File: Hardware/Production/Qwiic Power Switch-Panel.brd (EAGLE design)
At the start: 149.1 x 149.1 mm, 1505 parts, among them J1 Qwiic Right Angle, J10 PTH, J100 PTH, J103 Qwiic Right Angle, J104 PTH, J105 Qwiic Right Angle, J106 PTH, J109 Qwiic Right Angle, J110 PTH, J111 Qwiic Right Angle, J112 PTH, J115 Qwiic Right Angle, J116 PTH, J117 Qwiic Right Angle, J118 PTH, J121 Qwiic Right Angle, J122 PTH, J123 Qwiic Right Angle, J124 PTH, J127 Qwiic Right Angle, J128 PTH, J129 Qwiic Right Angle, J13 Qwiic Right Angle, J130 PTH, J133 Qwiic Right Angle, J134 PTH, J135 Qwiic Right Angle, J136 PTH, J139 Qwiic Right Angle, J14 PTH, J140 PTH, J141 Qwiic Right Angle, J142 PTH, J145 Qwiic Right Angle, J146 PTH, J147 Qwiic Right Angle, J148 PTH, J15 Qwiic Right Angle, J16 PTH, J19 Qwiic Right Angle, J2 PTH, J20 PTH, J21 Qwiic Right Angle, J22 PTH, J25 Qwiic Right Angle, J26 PTH, J27 Qwiic Right Angle, J28 PTH, J3 Qwiic Right Angle, J31 Qwiic Right Angle, J32 PTH, J33 Qwiic Right Angle, J34 PTH, J37 Qwiic Right Angle, J38 PTH, J39 Qwiic Right Angle, J4 PTH, J40 PTH, J43 Qwiic Right Angle, J44 PTH, J45 Qwiic Right Angle, J46 PTH, J49 Qwiic Right Angle, J50 PTH, J51 Qwiic Right Angle, J52 PTH, J55 Qwiic Right Angle, J56 PTH, J57 Qwiic Right Angle, J58 PTH, J61 Qwiic Right Angle, J62 PTH, J63 Qwiic Right Angle, J64 PTH, J67 Qwiic Right Angle, J68 PTH, J69 Qwiic Right Angle, J7 Qwiic Right Angle, J70 PTH, J73 Qwiic Right Angle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

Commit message: Add x02 production files
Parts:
- added I2C_OUT, I2C_OUT1, I2C_OUT10, I2C_OUT11, I2C_OUT12, I2C_OUT13, I2C_OUT14, I2C_OUT15, I2C_OUT16, I2C_OUT17, I2C_OUT18, I2C_OUT19, I2C_OUT2, I2C_OUT20, I2C_OUT21, I2C_OUT22, I2C_OUT23, I2C_OUT24, I2C_OUT3, I2C_OUT4, I2C_OUT5, I2C_OUT6, I2C_OUT7, I2C_OUT8, I2C_OUT9: JUMPER-SMT_3_2-NC_TRACE_SILK, SparkFun-Jumpers:SMT-JUMPER_3_2-NC_TRACE_SILK
- added R126, R127, R129, R130, R134, R135, R137, R138, R142, R143, R145, R146, R150, R151, R153, R154, R158, R159, R161, R162, R166, R167, R169, R170, R174, R175, R177, R178, R182, R183, R185, R186, R190, R191, R193, R194, R198, R199: 2.2k, SparkFun-Resistors:0603
- added R128, R136, R144, R152, R160, R168, R176, R184, R192, R200: 200k, SparkFun-Resistors:0603
- added R131, R133, R139, R141, R147, R149, R155, R157, R163, R165, R171, R173, R179, R181, R187, R189, R195, R197: 1k, SparkFun-Resistors:0603
- added R132, R140, R148, R156, R164, R172, R180, R188, R196: 470, SparkFun-Resistors:0603
- added U$776, U$800: (no value), Labels:I_SUPER2_C-()-03
- added U$777, U$780: (no value), Labels-0_04:GND1
- added U$778, U$782: (no value), Labels-0_04:SCL9
- added U$779, U$781: (no value), Labels-0_04:SDA8
- added U$783: (no value), Qwiic:QWIIC0
- added U$784, U$797: (no value), 3.3V_Flagtail:3#3V0
- added U$785, U$796: (no value), 3.3V_Pointer:3#3V0
- added U$786, U$794: (no value), GPIO1:GPIO10
- added U$787, U$795: (no value), GPIO2:GPIO20
- added U$788: (no value), IN:IN0
- added U$789: (no value), LED_IN:LED_IN0
- added U$790: (no value), LED_OUT:LED_OUT0
- added U$791: (no value), OUT:OUT0
- added U$792: (no value), Power:POWER0
- added U$793: (no value), Switch:SWITCH0
- added U$798: (no value), IN__3:IN0
- added U$799: (no value), OUT__3:OUT0
- added U51, U54, U57, U60, U63, U66, U69, U72, U75: (no value), SparkFun-IC-Comms:VSSOP_8PIN
- added U52, U55, U58, U61, U64, U67, U70, U73: PCA9536, New_Parts:MSOP8
- added U53, U56, U59, U62, U65, U68, U71, U74: 74HC1G04, SparkFun-IC-Logic:SOT353
- R10, R103, R105, R110, R113, R114, R118, R119, R14, R15, R18, R23, R25, R30, R33, R34, R38, R39, R49, R50, R54, R55, R58, R63, R65, R70, R73, R74, R78, R79, R89, R9, R90, R94, R95, R98: value 1k -> 2.2k
- R100, R108, R124, R2, R20, R28, R44, R60, R68, R84: value 1k -> 470
- R101, R107, R11, R117, R21, R27, R37, R51, R61, R67, R77, R91: value 2.2k -> 1k
- R104, R120, R24, R40, R48, R64, R8, R80, R88: value 1k -> 200k
- R112, R16, R32, R56, R72, R96: value 2.2k -> 200k
- R116, R12, R36, R52, R76, R92: value 2.2k -> 470
- U$1, U$94: value SPARKX-LOGO4 -> (none); device SparkX:SPARKX-MEDIUM -> IN__3:IN0
- U$100, U$107, U$134, U$196, U$262, U$324, U$38, U$45, U$685, U$747: device Labels-0_04:SCL9 -> Labels-0_04:SDA8
- U$101, U$194: device Labels:I_SUPER2_C-()-03 -> Labels-0_04:GND1
- U$102, U$164, U$198, U$260, U$36, U$43, U$653, U$715, U$749: device Labels-0_04:GND1 -> Labels-0_04:SDA8
- U$104, U$128, U$168, U$192, U$352, U$416: device Labels-0_04:SDA8 -> Labels:I_SUPER2_C-()-03
- U$106, U$135, U$199, U$259, U$323, U$35, U$42, U$686, U$750, U$99: device Labels-0_04:SDA8 -> Labels-0_04:SCL9
- U$108, U$201, U$325, U$418: device Qwiic:QWIIC0 -> Labels-0_04:GND1
- U$109, U$171, U$326, U$388, U$525, U$587, U$742: device 3.3V_Flagtail:3#3V0 -> Labels-0_04:SDA8
- U$110, U$234, U$327, U$451, U$462, U$586, U$679: device 3.3V_Pointer:3#3V0 -> Labels-0_04:SCL9
- U$111, U$367: device GPIO1:GPIO10 -> Qwiic:QWIIC0
- U$112, U$368, U$701: device GPIO2:GPIO20 -> 3.3V_Flagtail:3#3V0
- U$113, U$433, U$764, U$92: device IN:IN0 -> 3.3V_Pointer:3#3V0
- U$114: device LED_IN:LED_IN0 -> GPIO1:GPIO10
- U$115: device LED_OUT:LED_OUT0 -> GPIO2:GPIO20
- U$116, U$372: device OUT:OUT0 -> IN:IN0
- U$117: device Power:POWER0 -> LED_IN:LED_IN0
- U$118: device Switch:SWITCH0 -> LED_OUT:LED_OUT0
- U$119: device GPIO1:GPIO10 -> OUT:OUT0
- U$120: device GPIO2:GPIO20 -> Power:POWER0
- U$121, U$761: device 3.3V_Pointer:3#3V0 -> Switch:SWITCH0
- U$122, U$370, U$698: device 3.3V_Flagtail:3#3V0 -> GPIO1:GPIO10
- U$123, U$371, U$51: device IN:IN0 -> GPIO2:GPIO20
- U$124, U$209, U$465: device OUT:OUT0 -> 3.3V_Pointer:3#3V0
- U$125, U$528: value SPARKX-LOGO4 -> (none); device SparkX:SPARKX-MEDIUM -> 3.3V_Flagtail:3#3V0
- U$126, U$222, U$350, U$446: device Labels-0_04:GND1 -> IN__3:IN0
- U$127, U$255, U$351, U$479: device Labels-0_04:SCL9 -> OUT__3:OUT0
- U$129, U$257, U$353: value (none) -> SPARKX-LOGO4; device Labels-0_04:GND1 -> SparkX:SPARKX-MEDIUM
- U$130, U$137, U$197, U$261, U$290, U$354, U$37, U$44, U$66, U$73, U$748: device Labels-0_04:SDA8 -> Labels-0_04:GND1
- U$132, U$70: device Labels:I_SUPER2_C-()-03 -> Labels-0_04:SDA8
- U$136, U$160, U$18, U$288, U$384, U$40, U$64: device Labels-0_04:GND1 -> Labels:I_SUPER2_C-()-03
- U$139, U$294, U$356, U$77: device Qwiic:QWIIC0 -> Labels-0_04:SDA8
- U$14, U$671: device IN:IN0 -> OUT__3:OUT0
- U$140, U$233, U$357, U$450, U$556, U$649, U$773: device 3.3V_Flagtail:3#3V0 -> Labels-0_04:GND1
- U$141, U$203, U$358, U$420, U$493, U$555, U$710, U$772: device 3.3V_Pointer:3#3V0 -> Labels-0_04:SDA8
- U$142, U$266, U$359, U$398, U$483, U$522, U$615, U$739: device GPIO1:GPIO10 -> Labels-0_04:SCL9
- U$143, U$399: device GPIO2:GPIO20 -> Qwiic:QWIIC0
- U$144, U$464, U$61, U$733: device IN:IN0 -> 3.3V_Flagtail:3#3V0
- U$145: device LED_IN:LED_IN0 -> 3.3V_Pointer:3#3V0
- U$146: device LED_OUT:LED_OUT0 -> GPIO1:GPIO10
- U$147, U$155, U$403: device OUT:OUT0 -> GPIO2:GPIO20
- U$148: device Power:POWER0 -> IN:IN0
- U$149: device Switch:SWITCH0 -> LED_IN:LED_IN0
- U$150: device GPIO1:GPIO10 -> LED_OUT:LED_OUT0
- U$151: device GPIO2:GPIO20 -> OUT:OUT0
- U$152: device 3.3V_Pointer:3#3V0 -> Power:POWER0
- U$153, U$729: device 3.3V_Flagtail:3#3V0 -> Switch:SWITCH0
- U$154, U$402, U$82: device IN:IN0 -> GPIO1:GPIO10
- U$156, U$497: value SPARKX-LOGO4 -> (none); device SparkX:SPARKX-MEDIUM -> 3.3V_Pointer:3#3V0
- U$157, U$253, U$381, U$477, U$560, U$656: device Labels-0_04:GND1 -> 3.3V_Flagtail:3#3V0
- U$158, U$286, U$382, U$510: device Labels-0_04:SCL9 -> IN__3:IN0
- U$159, U$223, U$383, U$447: device Labels-0_04:SDA8 -> OUT__3:OUT0
- U$161, U$321, U$385, U$97: value (none) -> SPARKX-LOGO4; device Labels-0_04:SDA8 -> SparkX:SPARKX-MEDIUM
- U$162, U$165, U$169, U$258, U$293, U$33, U$386, U$41, U$69, U$716, U$76: device Labels-0_04:SCL9 -> Labels-0_04:GND1
- U$163, U$39: device Labels:I_SUPER2_C-()-03 -> Labels-0_04:SCL9
- U$167, U$195, U$291, U$622, U$67, U$71, U$718, U$74, U$746: device Labels-0_04:GND1 -> Labels-0_04:SCL9
- U$170, U$263, U$387, U$46: device Qwiic:QWIIC0 -> Labels-0_04:SCL9
- U$172, U$265, U$389, U$482, U$524, U$617, U$741: device 3.3V_Pointer:3#3V0 -> Labels-0_04:GND1
- U$173, U$235, U$390, U$429, U$452, U$491, U$646, U$708: device GPIO1:GPIO10 -> Labels-0_04:SDA8
- U$174, U$298, U$391, U$430, U$515, U$554, U$647, U$771: device GPIO2:GPIO20 -> Labels-0_04:SCL9
- U$175, U$495: device IN:IN0 -> Qwiic:QWIIC0
- U$176, U$765: device LED_IN:LED_IN0 -> 3.3V_Flagtail:3#3V0
- U$177: device LED_OUT:LED_OUT0 -> 3.3V_Pointer:3#3V0
- U$178, U$186, U$434: device OUT:OUT0 -> GPIO1:GPIO10
- U$179: device Power:POWER0 -> GPIO2:GPIO20
- U$180: device Switch:SWITCH0 -> IN:IN0
- U$181: device GPIO1:GPIO10 -> LED_IN:LED_IN0
- U$182: device GPIO2:GPIO20 -> LED_OUT:LED_OUT0
- U$183: device 3.3V_Pointer:3#3V0 -> OUT:OUT0
- U$184, U$760: device 3.3V_Flagtail:3#3V0 -> Power:POWER0
- U$185: device IN:IN0 -> Switch:SWITCH0
- U$187, U$435: value SPARKX-LOGO4 -> (none); device SparkX:SPARKX-MEDIUM -> GPIO2:GPIO20
- U$188, U$284, U$412, U$508, U$529, U$625, U$753: device Labels-0_04:GND1 -> 3.3V_Pointer:3#3V0
- U$189, U$317, U$413, U$541, U$592, U$720: device Labels-0_04:SCL9 -> 3.3V_Flagtail:3#3V0
- U$190, U$254, U$414, U$478: device Labels-0_04:SDA8 -> IN__3:IN0
- U$191, U$319, U$415, U$95: device Labels-0_04:GND1 -> OUT__3:OUT0
- U$193, U$289, U$417, U$65: value (none) -> SPARKX-LOGO4; device Labels-0_04:SCL9 -> SparkX:SPARKX-MEDIUM
- U$200, U$224, U$320, U$448, U$72, U$96: device Labels-0_04:SCL9 -> Labels:I_SUPER2_C-()-03
- U$202, U$295, U$419, U$494, U$618, U$711, U$78: device 3.3V_Flagtail:3#3V0 -> Labels-0_04:SCL9
- U$204, U$297, U$421, U$460, U$514, U$553, U$677, U$770: device GPIO1:GPIO10 -> Labels-0_04:GND1
- U$205, U$267, U$422, U$461, U$484, U$523, U$678, U$740: device GPIO2:GPIO20 -> Labels-0_04:SDA8
- U$206, U$330, U$423, U$526, U$547, U$650, U$743: device IN:IN0 -> Labels-0_04:SCL9
- U$207: device LED_IN:LED_IN0 -> Qwiic:QWIIC0
- U$208: device LED_OUT:LED_OUT0 -> 3.3V_Flagtail:3#3V0
- U$21, U$705: value (none) -> SPARKX-LOGO4; device OUT:OUT0 -> SparkX:SPARKX-MEDIUM
- U$210: device Power:POWER0 -> GPIO1:GPIO10
- U$211: device Switch:SWITCH0 -> GPIO2:GPIO20
- U$212: device GPIO1:GPIO10 -> IN:IN0
- U$213: device GPIO2:GPIO20 -> LED_IN:LED_IN0
- U$214: device 3.3V_Pointer:3#3V0 -> LED_OUT:LED_OUT0
- U$215: device 3.3V_Flagtail:3#3V0 -> OUT:OUT0
- U$216: device IN:IN0 -> Power:POWER0
- U$217: device OUT:OUT0 -> Switch:SWITCH0
- U$218, U$466: value SPARKX-LOGO4 -> (none); device SparkX:SPARKX-MEDIUM -> GPIO1:GPIO10
- U$219, U$315, U$443, U$467, U$539, U$563, U$691: device Labels-0_04:GND1 -> GPIO2:GPIO20
- U$220, U$348, U$444, U$561, U$572, U$689: device Labels-0_04:SCL9 -> 3.3V_Pointer:3#3V0
- U$221, U$285, U$445, U$509, U$624, U$688: device Labels-0_04:SDA8 -> 3.3V_Flagtail:3#3V0
- U$225: value (none) -> SPARKX-LOGO4; device Labels:I_SUPER2_C-()-03 -> SparkX:SPARKX-MEDIUM
- U$232, U$480: device Qwiic:QWIIC0 -> Labels:I_SUPER2_C-()-03
- U$236, U$329, U$453, U$492, U$546, U$585, U$709: device GPIO2:GPIO20 -> Labels-0_04:GND1
- U$237, U$299, U$454, U$516, U$557, U$619, U$774: device IN:IN0 -> Labels-0_04:SDA8
- U$238, U$362, U$455, U$579: device LED_IN:LED_IN0 -> Labels-0_04:SCL9
- U$239: device LED_OUT:LED_OUT0 -> Qwiic:QWIIC0
- U$240, U$496, U$93: device OUT:OUT0 -> 3.3V_Flagtail:3#3V0
- U$241: device Power:POWER0 -> 3.3V_Pointer:3#3V0
- U$242: device Switch:SWITCH0 -> GPIO1:GPIO10
- U$243, U$731: device GPIO1:GPIO10 -> GPIO2:GPIO20
- U$244: device GPIO2:GPIO20 -> IN:IN0
- U$245: device 3.3V_Pointer:3#3V0 -> LED_IN:LED_IN0
- U$246: device 3.3V_Flagtail:3#3V0 -> LED_OUT:LED_OUT0
- U$247: device IN:IN0 -> OUT:OUT0
- U$248: device OUT:OUT0 -> Power:POWER0
- U$249: value SPARKX-LOGO4 -> (none); device SparkX:SPARKX-MEDIUM -> Switch:SWITCH0
- U$250, U$346, U$474, U$498, U$570, U$594, U$722: device Labels-0_04:GND1 -> GPIO1:GPIO10
- U$251, U$379, U$475, U$499, U$603, U$627, U$723: device Labels-0_04:SCL9 -> GPIO2:GPIO20
- U$252, U$316, U$476, U$540, U$593, U$657: device Labels-0_04:SDA8 -> 3.3V_Pointer:3#3V0
- U$264, U$512, U$680: device 3.3V_Flagtail:3#3V0 -> Labels:I_SUPER2_C-()-03
- U$268, U$361, U$485, U$578, U$588, U$681: device IN:IN0 -> Labels-0_04:GND1
- U$269, U$331, U$486, U$548: device LED_IN:LED_IN0 -> Labels-0_04:SDA8
- U$270, U$394, U$487, U$611: device LED_OUT:LED_OUT0 -> Labels-0_04:SCL9
- U$271, U$527: device OUT:OUT0 -> Qwiic:QWIIC0
- U$272: device Power:POWER0 -> 3.3V_Flagtail:3#3V0
- U$273: device Switch:SWITCH0 -> 3.3V_Pointer:3#3V0
- U$276: device 3.3V_Pointer:3#3V0 -> IN:IN0
- U$277: device 3.3V_Flagtail:3#3V0 -> LED_IN:LED_IN0
- U$278: device IN:IN0 -> LED_OUT:LED_OUT0
- U$280: value SPARKX-LOGO4 -> (none); device SparkX:SPARKX-MEDIUM -> Power:POWER0
- U$281, U$377, U$505, U$601: device Labels-0_04:GND1 -> Switch:SWITCH0
- U$282, U$410, U$506, U$530, U$634, U$658, U$754: device Labels-0_04:SCL9 -> GPIO1:GPIO10
- U$283, U$347, U$507, U$531, U$571, U$595, U$755: device Labels-0_04:SDA8 -> GPIO2:GPIO20
- U$287: device Labels:I_SUPER2_C-()-03 -> OUT__3:OUT0
- U$296, U$544, U$648: device 3.3V_Pointer:3#3V0 -> Labels:I_SUPER2_C-()-03
- U$300, U$393, U$517, U$610: device LED_IN:LED_IN0 -> Labels-0_04:GND1
- U$301, U$363, U$518, U$580: device LED_OUT:LED_OUT0 -> Labels-0_04:SDA8
- U$302, U$426, U$519, U$558, U$643, U$682, U$775: device OUT:OUT0 -> Labels-0_04:SCL9
- U$303: device Power:POWER0 -> Qwiic:QWIIC0
- U$304: device Switch:SWITCH0 -> 3.3V_Flagtail:3#3V0
- U$305, U$49, U$700: device GPIO1:GPIO10 -> 3.3V_Pointer:3#3V0
- U$306, U$50, U$58: device GPIO2:GPIO20 -> GPIO1:GPIO10
- U$307, U$59, U$699: device 3.3V_Pointer:3#3V0 -> GPIO2:GPIO20
- U$308: device 3.3V_Flagtail:3#3V0 -> IN:IN0
- U$309: device IN:IN0 -> LED_IN:LED_IN0
- U$310, U$54: device OUT:OUT0 -> LED_OUT:LED_OUT0
- U$311: value SPARKX-LOGO4 -> (none); device SparkX:SPARKX-MEDIUM -> OUT:OUT0
- U$312, U$408, U$536, U$632: device Labels-0_04:GND1 -> Power:POWER0
- U$313, U$441, U$537, U$665: device Labels-0_04:SCL9 -> Switch:SWITCH0
- U$314, U$378, U$538, U$562, U$602, U$626: device Labels-0_04:SDA8 -> GPIO1:GPIO10
- U$318: device Labels:I_SUPER2_C-()-03 -> IN__3:IN0
- U$328, U$576, U$584: device GPIO1:GPIO10 -> Labels:I_SUPER2_C-()-03
- U$332, U$425, U$549, U$642: device LED_OUT:LED_OUT0 -> Labels-0_04:GND1
- U$333, U$395, U$550, U$589, U$612, U$651: device OUT:OUT0 -> Labels-0_04:SDA8
- U$334, U$458, U$551, U$675: device Power:POWER0 -> Labels-0_04:SCL9
- U$335: device Switch:SWITCH0 -> Qwiic:QWIIC0
- U$336, U$669, U$80: device GPIO1:GPIO10 -> 3.3V_Flagtail:3#3V0
- U$337, U$732, U$81: device GPIO2:GPIO20 -> 3.3V_Pointer:3#3V0
- U$338, U$730, U$90: device 3.3V_Pointer:3#3V0 -> GPIO1:GPIO10
- U$339, U$667, U$91: device 3.3V_Flagtail:3#3V0 -> GPIO2:GPIO20
- U$341, U$85: device OUT:OUT0 -> LED_IN:LED_IN0
- U$342: value SPARKX-LOGO4 -> (none); device SparkX:SPARKX-MEDIUM -> LED_OUT:LED_OUT0
- U$343, U$439, U$567, U$663: device Labels-0_04:GND1 -> OUT:OUT0
- U$344, U$472, U$568, U$696: device Labels-0_04:SCL9 -> Power:POWER0
- U$345, U$409, U$569, U$633: device Labels-0_04:SDA8 -> Switch:SWITCH0
- U$349, U$752: device Labels:I_SUPER2_C-()-03 -> 3.3V_Flagtail:3#3V0
- U$360, U$608, U$616: device GPIO2:GPIO20 -> Labels:I_SUPER2_C-()-03
- U$364, U$457, U$581, U$620, U$674, U$713: device OUT:OUT0 -> Labels-0_04:GND1
- U$365, U$427, U$582, U$644: device Power:POWER0 -> Labels-0_04:SDA8
- U$366, U$490, U$583, U$707: device Switch:SWITCH0 -> Labels-0_04:SCL9
- U$373: value SPARKX-LOGO4 -> (none); device SparkX:SPARKX-MEDIUM -> LED_IN:LED_IN0
- U$374, U$470, U$598, U$694: device Labels-0_04:GND1 -> LED_OUT:LED_OUT0
- U$375, U$503, U$599, U$727: device Labels-0_04:SCL9 -> OUT:OUT0
- U$376, U$440, U$600, U$664: device Labels-0_04:SDA8 -> Power:POWER0
- U$380, U$721: device Labels:I_SUPER2_C-()-03 -> 3.3V_Pointer:3#3V0
- U$392, U$640, U$712: device IN:IN0 -> Labels:I_SUPER2_C-()-03
- U$396, U$489, U$613, U$706: device Power:POWER0 -> Labels-0_04:GND1
- U$397, U$459, U$614, U$676: device Switch:SWITCH0 -> Labels-0_04:SDA8
- U$400, U$48, U$637: device 3.3V_Pointer:3#3V0 -> 3.3V_Flagtail:3#3V0
- U$401, U$60, U$636: device 3.3V_Flagtail:3#3V0 -> 3.3V_Pointer:3#3V0
- U$404: value SPARKX-LOGO4 -> (none); device SparkX:SPARKX-MEDIUM -> IN:IN0
- U$405, U$501, U$629, U$725: device Labels-0_04:GND1 -> LED_IN:LED_IN0
- U$406, U$534, U$630, U$758: device Labels-0_04:SCL9 -> LED_OUT:LED_OUT0
- U$407, U$471, U$631, U$695: device Labels-0_04:SDA8 -> OUT:OUT0
- U$411, U$659: device Labels:I_SUPER2_C-()-03 -> GPIO2:GPIO20
- U$424, U$672: device LED_IN:LED_IN0 -> Labels:I_SUPER2_C-()-03
- U$428, U$521, U$645, U$738: device Switch:SWITCH0 -> Labels-0_04:GND1
- U$431, U$79: device 3.3V_Pointer:3#3V0 -> Qwiic:QWIIC0
- U$436, U$532, U$660, U$756: device Labels-0_04:GND1 -> IN:IN0
- U$437, U$565, U$661: device Labels-0_04:SCL9 -> LED_IN:LED_IN0
- U$438, U$502, U$662, U$726: device Labels-0_04:SDA8 -> LED_OUT:LED_OUT0
- U$442, U$690: device Labels:I_SUPER2_C-()-03 -> GPIO1:GPIO10
- U$449: value (none) -> SPARKX-LOGO4; device Qwiic:QWIIC0 -> SparkX:SPARKX-MEDIUM
- U$456, U$704: device LED_OUT:LED_OUT0 -> Labels:I_SUPER2_C-()-03
- U$463, U$47: device 3.3V_Flagtail:3#3V0 -> Qwiic:QWIIC0
- U$468, U$596, U$692: device Labels-0_04:SCL9 -> IN:IN0
- U$469, U$533, U$693, U$757: device Labels-0_04:SDA8 -> LED_IN:LED_IN0
- U$473: device Labels:I_SUPER2_C-()-03 -> Switch:SWITCH0
- U$481: value (none) -> SPARKX-LOGO4; device 3.3V_Flagtail:3#3V0 -> SparkX:SPARKX-MEDIUM
- U$488, U$736, U$744: device OUT:OUT0 -> Labels:I_SUPER2_C-()-03
- U$500, U$564, U$724: device Labels-0_04:SDA8 -> IN:IN0
- U$504: device Labels:I_SUPER2_C-()-03 -> Power:POWER0
- U$511: device Qwiic:QWIIC0 -> OUT__3:OUT0
- U$513: value (none) -> SPARKX-LOGO4; device 3.3V_Pointer:3#3V0 -> SparkX:SPARKX-MEDIUM
- U$52: device LED_IN:LED_IN0 -> IN:IN0
- U$520, U$768: device Power:POWER0 -> Labels:I_SUPER2_C-()-03
- U$53: device LED_OUT:LED_OUT0 -> LED_IN:LED_IN0
- U$535: device Labels:I_SUPER2_C-()-03 -> OUT:OUT0
- U$542: device Qwiic:QWIIC0 -> IN__3:IN0
- U$543: device 3.3V_Flagtail:3#3V0 -> OUT__3:OUT0
- U$545: value (none) -> SPARKX-LOGO4; device GPIO1:GPIO10 -> SparkX:SPARKX-MEDIUM
- U$55: device Power:POWER0 -> OUT:OUT0
- U$552: device Switch:SWITCH0 -> Labels:I_SUPER2_C-()-03
- U$559: value SPARKX-LOGO4 -> (none); device SparkX:SPARKX-MEDIUM -> Qwiic:QWIIC0
- U$56: device Switch:SWITCH0 -> Power:POWER0
- U$566: device Labels:I_SUPER2_C-()-03 -> LED_OUT:LED_OUT0
- U$57: device GPIO1:GPIO10 -> Switch:SWITCH0
- U$573: device Qwiic:QWIIC0 -> 3.3V_Flagtail:3#3V0
- U$574: device 3.3V_Flagtail:3#3V0 -> IN__3:IN0
- U$575: device 3.3V_Pointer:3#3V0 -> OUT__3:OUT0
- U$577: value (none) -> SPARKX-LOGO4; device GPIO2:GPIO20 -> SparkX:SPARKX-MEDIUM
- U$590, U$714: value SPARKX-LOGO4 -> (none); device SparkX:SPARKX-MEDIUM -> Labels-0_04:SCL9
- U$591, U$687: device Labels-0_04:GND1 -> Qwiic:QWIIC0
- U$597: device Labels:I_SUPER2_C-()-03 -> LED_IN:LED_IN0
- U$604: device Qwiic:QWIIC0 -> 3.3V_Pointer:3#3V0
- U$606: device 3.3V_Pointer:3#3V0 -> IN__3:IN0
- U$607: device GPIO1:GPIO10 -> OUT__3:OUT0
- U$609: value (none) -> SPARKX-LOGO4; device IN:IN0 -> SparkX:SPARKX-MEDIUM
- U$62: device OUT:OUT0 -> IN__3:IN0
- U$621, U$683: value SPARKX-LOGO4 -> (none); device SparkX:SPARKX-MEDIUM -> Labels-0_04:SDA8
- U$623, U$751: device Labels-0_04:SCL9 -> Qwiic:QWIIC0
- U$628: device Labels:I_SUPER2_C-()-03 -> IN:IN0
- U$63: value SPARKX-LOGO4 -> (none); device SparkX:SPARKX-MEDIUM -> OUT__3:OUT0
- U$635: device Qwiic:QWIIC0 -> GPIO2:GPIO20
- U$638: device GPIO1:GPIO10 -> IN__3:IN0
- U$639: device GPIO2:GPIO20 -> OUT__3:OUT0
- U$641: value (none) -> SPARKX-LOGO4; device LED_IN:LED_IN0 -> SparkX:SPARKX-MEDIUM
- U$652, U$745: value SPARKX-LOGO4 -> (none); device SparkX:SPARKX-MEDIUM -> Labels-0_04:GND1
- U$655, U$719: device Labels-0_04:SDA8 -> Qwiic:QWIIC0
- U$666: device Qwiic:QWIIC0 -> GPIO1:GPIO10
- U$670: device GPIO2:GPIO20 -> IN__3:IN0
- U$673: value (none) -> SPARKX-LOGO4; device LED_OUT:LED_OUT0 -> SparkX:SPARKX-MEDIUM
- U$697: device Qwiic:QWIIC0 -> Switch:SWITCH0
- U$702: device IN:IN0 -> IN__3:IN0
- U$703: device LED_IN:LED_IN0 -> OUT__3:OUT0
- U$728: device Qwiic:QWIIC0 -> Power:POWER0
- U$734: device LED_IN:LED_IN0 -> IN__3:IN0
- U$735: device LED_OUT:LED_OUT0 -> OUT__3:OUT0
- U$737: value (none) -> SPARKX-LOGO4; device Power:POWER0 -> SparkX:SPARKX-MEDIUM
- U$759: device Qwiic:QWIIC0 -> OUT:OUT0
- U$766: device LED_OUT:LED_OUT0 -> IN__3:IN0
- U$767: device OUT:OUT0 -> OUT__3:OUT0
- U$769: value (none) -> SPARKX-LOGO4; device Switch:SWITCH0 -> SparkX:SPARKX-MEDIUM
- U$83: device LED_IN:LED_IN0 -> GPIO2:GPIO20
- U$84: device LED_OUT:LED_OUT0 -> IN:IN0
- U$86: device Power:POWER0 -> LED_OUT:LED_OUT0
- U$87: device Switch:SWITCH0 -> OUT:OUT0
- U$88: device GPIO1:GPIO10 -> Power:POWER0
- U$89: device GPIO2:GPIO20 -> Switch:SWITCH0
- U10, U16, U22, U28, U34, U4, U40, U46: value 74HC1G04 -> PCA9536; device SparkFun-IC-Logic:SOT353 -> New_Parts:MSOP8
- U11, U17, U23, U29, U35, U41, U47, U5: value PCA9536 -> 74HC1G04; device New_Parts:MSOP8 -> SparkFun-IC-Logic:SOT353
- U12, U18, U24, U30, U36, U42, U48, U6: value 74HC1G04 -> (none); device SparkFun-IC-Logic:SOT353 -> SparkFun-IC-Comms:VSSOP_8PIN
- U15, U21, U27, U3, U33, U39, U45, U9: value PCA9536 -> (none); device New_Parts:MSOP8 -> SparkFun-IC-Comms:VSSOP_8PIN
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- renumbered I2C to I2C_IN, I2C1 to I2C_IN1, I2C10 to I2C_IN10, I2C11 to I2C_IN11, I2C12 to I2C_IN12, I2C13 to I2C_IN13, I2C14 to I2C_IN14, I2C15 to I2C_IN15, I2C16 to I2C_IN16, I2C17 to I2C_IN17, I2C18 to I2C_IN18, I2C19 to I2C_IN19, I2C2 to I2C_IN2, I2C20 to I2C_IN20, I2C21 to I2C_IN21, I2C22 to I2C_IN22, I2C23 to I2C_IN23, I2C24 to I2C_IN24, I2C3 to I2C_IN3, I2C4 to I2C_IN4, I2C5 to I2C_IN5, I2C6 to I2C_IN6, I2C7 to I2C_IN7, I2C8 to I2C_IN8, I2C9 to I2C_IN9
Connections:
- new net GPIO75: U55.5, U57.P8
- new net GPIO76: U58.1, U59.2
- new net GPIO77: J119.1, U58.2
- new net GPIO78: J120.1, U58.3
- new net GPIO79: U58.5, U60.P8
- new net GPIO80: U61.1, U62.2
- new net GPIO81: J125.1, U61.2
- new net GPIO82: J126.1, U61.3
- new net GPIO83: U61.5, U63.P8
- new net GPIO84: U64.1, U65.2
- new net GPIO85: J131.1, U64.2
- new net GPIO86: J132.1, U64.3
- new net GPIO87: U64.5, U66.P8
- new net GPIO88: U67.1, U68.2
- new net GPIO89: J137.1, U67.2
- new net GPIO90: J138.1, U67.3
- new net GPIO91: U67.5, U69.P8
- new net GPIO92: U70.1, U71.2
- new net GPIO93: J143.1, U70.2
- new net GPIO94: J144.1, U70.3
- new net GPIO95: U70.5, U72.P8
- new net GPIO96: U73.1, U74.2
- new net GPIO97: J149.1, U73.2
- new net GPIO98: J150.1, U73.3
- new net GPIO99: U73.5, U75.P8
- new net N$201: D37.A, R147.1
- new net N$202: D38.A, R148.1
- new net N$203: IN_LED18.1, R147.2
- new net N$204: OUT_LED18.1, R148.2
- new net N$205: R149.1, U56.4
- new net N$206: Q19.1, R149.2
- new net N$207: I2C_OUT18.1, R151.2
- new net N$208: I2C_OUT18.3, R150.2
- new net N$209: R152.1, U57.P7
- new net N$210: I2C_IN19.1, R154.2
- new net N$211: I2C_IN19.3, R153.2
- new net N$212: D39.A, R155.1
- new net N$213: D40.A, R156.1
- new net N$214: IN_LED19.1, R155.2
- new net N$215: OUT_LED19.1, R156.2
- new net N$216: R157.1, U59.4
- new net N$217: Q20.1, R157.2
- new net N$218: I2C_OUT19.1, R159.2
- new net N$219: I2C_OUT19.3, R158.2
- new net N$220: R160.1, U60.P7
- new net N$221: I2C_IN20.1, R162.2
- new net N$222: I2C_IN20.3, R161.2
- new net N$223: D41.A, R163.1
- new net N$224: D42.A, R164.1
- new net N$225: IN_LED20.1, R163.2
- new net N$226: OUT_LED20.1, R164.2
- new net N$227: R165.1, U62.4
- new net N$228: Q21.1, R165.2
- new net N$229: I2C_OUT20.1, R167.2
- new net N$230: I2C_OUT20.3, R166.2
- new net N$231: R168.1, U63.P7
- new net N$232: I2C_IN21.1, R170.2
- new net N$233: I2C_IN21.3, R169.2
- new net N$234: D43.A, R171.1
- new net N$235: D44.A, R172.1
- new net N$236: IN_LED21.1, R171.2
- new net N$237: OUT_LED21.1, R172.2
- new net N$238: R173.1, U65.4
- new net N$239: Q22.1, R173.2
- new net N$240: I2C_OUT21.1, R175.2
- new net N$241: I2C_OUT21.3, R174.2
- new net N$242: R176.1, U66.P7
- new net N$243: I2C_IN22.1, R178.2
- new net N$244: I2C_IN22.3, R177.2
- new net N$245: D45.A, R179.1
- new net N$246: D46.A, R180.1
- new net N$247: IN_LED22.1, R179.2
- new net N$248: OUT_LED22.1, R180.2
- new net N$249: R181.1, U68.4
- new net N$250: Q23.1, R181.2
- new net N$251: I2C_OUT22.1, R183.2
- new net N$252: I2C_OUT22.3, R182.2
- new net N$253: R184.1, U69.P7
- new net N$254: I2C_IN23.1, R186.2
- new net N$255: I2C_IN23.3, R185.2
- new net N$256: D47.A, R187.1
- new net N$257: D48.A, R188.1
- new net N$258: IN_LED23.1, R187.2
- new net N$259: OUT_LED23.1, R188.2
- new net N$260: R189.1, U71.4
- new net N$261: Q24.1, R189.2
- new net N$262: I2C_OUT23.1, R191.2
- new net N$263: I2C_OUT23.3, R190.2
- new net N$264: R192.1, U72.P7
- new net N$265: I2C_IN24.1, R194.2
- new net N$266: I2C_IN24.3, R193.2
- new net N$267: D49.A, R195.1
- new net N$268: D50.A, R196.1
- new net N$269: IN_LED24.1, R195.2
- new net N$270: OUT_LED24.1, R196.2
- new net N$271: R197.1, U74.4
- new net N$272: Q25.1, R197.2
- new net N$273: I2C_OUT24.1, R199.2
- new net N$274: I2C_OUT24.3, R198.2
- new net N$275: R200.1, U75.P7
- new net SCL_OUT: J3.4, J4.4, R7.1, U3.P6
- new net SCL_OUT1: J10.4, J9.4, R15.1, U6.P6
- new net SCL_OUT10: J63.4, J64.4, R87.1, U33.P6
- new net SCL_OUT11: J69.4, J70.4, R95.1, U36.P6
- new net SCL_OUT12: J75.4, J76.4, R103.1, U39.P6
- new net SCL_OUT13: J81.4, J82.4, R111.1, U42.P6
- new net SCL_OUT14: J87.4, J88.4, R119.1, U45.P6
- new net SCL_OUT15: J93.4, J94.4, R127.1, U48.P6
- new net SCL_OUT16: J100.4, J99.4, R135.1, U51.P6
- new net SCL_OUT17: J105.4, J106.4, R143.1, U54.P6
- new net SCL_OUT18: J111.4, J112.4, R151.1, U57.P6
- new net SCL_OUT19: J117.4, J118.4, R159.1, U60.P6
- new net SCL_OUT2: J15.4, J16.4, R23.1, U9.P6
- new net SCL_OUT20: J123.4, J124.4, R167.1, U63.P6
- new net SCL_OUT21: J129.4, J130.4, R175.1, U66.P6
- new net SCL_OUT22: J135.4, J136.4, R183.1, U69.P6
- new net SCL_OUT23: J141.4, J142.4, R191.1, U72.P6
- new net SCL_OUT24: J147.4, J148.4, R199.1, U75.P6
- new net SCL_OUT3: J21.4, J22.4, R31.1, U12.P6
- new net SCL_OUT4: J27.4, J28.4, R39.1, U15.P6
- new net SCL_OUT5: J33.4, J34.4, R47.1, U18.P6
- new net SCL_OUT6: J39.4, J40.4, R55.1, U21.P6
- new net SCL_OUT7: J45.4, J46.4, R63.1, U24.P6
- new net SCL_OUT8: J51.4, J52.4, R71.1, U27.P6
- new net SCL_OUT9: J57.4, J58.4, R79.1, U30.P6
- new net SDA_OUT: J3.3, J4.3, R6.1, U3.P5
- new net SDA_OUT1: J10.3, J9.3, R14.1, U6.P5
- new net SDA_OUT10: J63.3, J64.3, R86.1, U33.P5
- new net SDA_OUT11: J69.3, J70.3, R94.1, U36.P5
- new net SDA_OUT12: J75.3, J76.3, R102.1, U39.P5
- new net SDA_OUT13: J81.3, J82.3, R110.1, U42.P5
- new net SDA_OUT14: J87.3, J88.3, R118.1, U45.P5
- new net SDA_OUT15: J93.3, J94.3, R126.1, U48.P5
- new net SDA_OUT16: J100.3, J99.3, R134.1, U51.P5
- new net SDA_OUT17: J105.3, J106.3, R142.1, U54.P5
- new net SDA_OUT18: J111.3, J112.3, R150.1, U57.P5
- new net SDA_OUT19: J117.3, J118.3, R158.1, U60.P5
- new net SDA_OUT2: J15.3, J16.3, R22.1, U9.P5
- new net SDA_OUT20: J123.3, J124.3, R166.1, U63.P5
- new net SDA_OUT21: J129.3, J130.3, R174.1, U66.P5
- new net SDA_OUT22: J135.3, J136.3, R182.1, U69.P5
- new net SDA_OUT23: J141.3, J142.3, R190.1, U72.P5
- new net SDA_OUT24: J147.3, J148.3, R198.1, U75.P5
- new net SDA_OUT3: J21.3, J22.3, R30.1, U12.P5
- new net SDA_OUT4: J27.3, J28.3, R38.1, U15.P5
- new net SDA_OUT5: J33.3, J34.3, R46.1, U18.P5
- new net SDA_OUT6: J39.3, J40.3, R54.1, U21.P5
- new net SDA_OUT7: J45.3, J46.3, R62.1, U24.P5
- new net SDA_OUT8: J51.3, J52.3, R70.1, U27.P5
- new net SDA_OUT9: J57.3, J58.3, R78.1, U30.P5
- net 3.3V: now also R8.2, U3.P2
- net 3.3V1: now also R16.2, U4.8, U5.5, U6.P2; no longer U3.8, U4.5
- net 3.3V10: now also R88.2, U31.8, U32.5, U33.P2; no longer U21.8, U22.5
- net 3.3V11: now also R96.2, U34.8, U35.5, U36.P2; no longer U23.8, U24.5
- net 3.3V12: now also R104.2, U37.8, U38.5, U39.P2; no longer U25.8, U26.5
- net 3.3V13: now also R112.2, U40.8, U41.5, U42.P2; no longer U27.8, U28.5
- net 3.3V14: now also R120.2, U43.8, U44.5, U45.P2; no longer U29.8, U30.5
- net 3.3V15: now also R128.2, U46.8, U47.5, U48.P2; no longer U31.8, U32.5
- net 3.3V16: now also R136.2, U49.8, U50.5, U51.P2; no longer U33.8, U34.5
- net 3.3V17: now also R144.2, U52.8, U53.5, U54.P2; no longer U35.8, U36.5
- net 3.3V18: now also R152.2, U55.8, U56.5, U57.P2; no longer U37.8, U38.5
- net 3.3V19: now also R160.2, U58.8, U59.5, U60.P2; no longer U39.8, U40.5
- net 3.3V2: now also R24.2, U7.8, U8.5, U9.P2; no longer U5.8, U6.5
- net 3.3V20: now also R168.2, U61.8, U62.5, U63.P2; no longer U41.8, U42.5
- net 3.3V21: now also R176.2, U64.8, U65.5, U66.P2; no longer U43.8, U44.5
- net 3.3V22: now also R184.2, U67.8, U68.5, U69.P2; no longer U45.8, U46.5
- net 3.3V23: now also R192.2, U70.8, U71.5, U72.P2; no longer U47.8, U48.5
- net 3.3V24: now also R200.2, U73.8, U74.5, U75.P2; no longer U49.8, U50.5
- net 3.3V3: now also R32.2, U10.8, U11.5, U12.P2; no longer U7.8, U8.5
- net 3.3V4: now also R40.2, U13.8, U14.5, U15.P2; no longer U10.5, U9.8
- net 3.3V5: now also R48.2, U16.8, U17.5, U18.P2; no longer U11.8, U12.5
- net 3.3V6: now also R56.2, U19.8, U20.5, U21.P2; no longer U13.8, U14.5
- net 3.3V7: now also R64.2, U22.8, U23.5, U24.P2; no longer U15.8, U16.5
- net 3.3V8: now also R72.2, U25.8, U26.5, U27.P2; no longer U17.8, U18.5
- net 3.3V9: now also R80.2, U28.8, U29.5, U30.P2; no longer U19.8, U20.5
- net GND: now also U3.P1
- net GND1: now also U4.4, U5.3, U6.P1; no longer U3.4, U4.3
- net GND10: now also U31.4, U32.3, U33.P1; no longer U21.4, U22.3
- net GND11: now also U34.4, U35.3, U36.P1; no longer U23.4, U24.3
- net GND12: now also U37.4, U38.3, U39.P1; no longer U25.4, U26.3
- net GND13: now also U40.4, U41.3, U42.P1; no longer U27.4, U28.3
- net GND14: now also U43.4, U44.3, U45.P1; no longer U29.4, U30.3
- net GND15: now also U46.4, U47.3, U48.P1; no longer U31.4, U32.3
- net GND16: now also U49.4, U50.3, U51.P1; no longer U33.4, U34.3
- net GND17: now also U52.4, U53.3, U54.P1; no longer U35.4, U36.3
- net GND18: now also U55.4, U56.3, U57.P1; no longer U37.4, U38.3
- net GND19: now also U58.4, U59.3, U60.P1; no longer U39.4, U40.3
- net GND2: now also U7.4, U8.3, U9.P1; no longer U5.4, U6.3
- net GND20: now also U61.4, U62.3, U63.P1; no longer U41.4, U42.3
- net GND21: now also U64.4, U65.3, U66.P1; no longer U43.4, U44.3
- net GND22: now also U67.4, U68.3, U69.P1; no longer U45.4, U46.3
- net GND23: now also U70.4, U71.3, U72.P1; no longer U47.4, U48.3
- net GND24: now also U73.4, U74.3, U75.P1; no longer U49.4, U50.3
- net GND3: now also U10.4, U11.3, U12.P1; no longer U7.4, U8.3
- net GND4: now also U13.4, U14.3, U15.P1; no longer U10.3, U9.4
- net GND5: now also U16.4, U17.3, U18.P1; no longer U11.4, U12.3
- net GND6: now also U19.4, U20.3, U21.P1; no longer U13.4, U14.3
- net GND7: now also U22.4, U23.3, U24.P1; no longer U15.4, U16.3
- net GND8: now also U25.4, U26.3, U27.P1; no longer U17.4, U18.3
- net GND9: now also U28.4, U29.3, U30.P1; no longer U19.4, U20.3
- net GPIO10: now also J18.1, U7.3; no longer J23.1, U7.2
- net GPIO11: now also U7.5, U9.P8; no longer J24.1, U7.3
- net GPIO12: now also U10.1, U11.2; no longer U10.2, U9.1
- net GPIO13: now also J23.1, U10.2; no longer J29.1, U9.2
- net GPIO14: now also J24.1, U10.3; no longer J30.1, U9.3
- net GPIO15: now also U10.5, U12.P8; no longer U11.1, U12.2
- net GPIO16: now also U13.1, U14.2; no longer J35.1, U11.2
- net GPIO17: now also J29.1, U13.2; no longer J36.1, U11.3
- net GPIO18: now also J30.1, U13.3; no longer U13.1, U14.2
- net GPIO19: now also U13.5, U15.P8; no longer J41.1, U13.2
- net GPIO20: now also U16.1, U17.2; no longer J42.1, U13.3
- net GPIO21: now also J35.1; no longer U15.1
- net GPIO22: now also J36.1, U16.3; no longer J47.1, U15.2
- net GPIO23: now also U16.5, U18.P8; no longer J48.1, U15.3
- net GPIO24: now also U19.1, U20.2; no longer U17.1, U18.2
- net GPIO25: now also J41.1, U19.2; no longer J53.1, U17.2
- net GPIO26: now also J42.1, U19.3; no longer J54.1, U17.3
- net GPIO27: now also U19.5, U21.P8; no longer U19.1, U20.2
- net GPIO28: now also U22.1, U23.2; no longer J59.1, U19.2
- net GPIO29: now also J47.1, U22.2; no longer J60.1, U19.3
- net GPIO3: now also U2.5, U3.P8; no longer U3.1, U4.2
- net GPIO30: now also J48.1, U22.3; no longer U21.1, U22.2
- net GPIO31: now also U22.5, U24.P8; no longer J65.1, U21.2
- net GPIO32: now also U25.1, U26.2; no longer J66.1, U21.3
- net GPIO33: now also J53.1, U25.2; no longer U23.1, U24.2
- net GPIO34: now also J54.1, U25.3; no longer J71.1, U23.2
- net GPIO35: now also U25.5, U27.P8; no longer J72.1, U23.3
- net GPIO36: now also U28.1, U29.2; no longer U25.1, U26.2
- net GPIO37: now also J59.1, U28.2; no longer J77.1, U25.2
- net GPIO38: now also J60.1, U28.3; no longer J78.1, U25.3
- net GPIO39: now also U28.5, U30.P8; no longer U27.1, U28.2
- net GPIO4: now also U4.1, U5.2; no longer J11.1, U3.2
- net GPIO40: now also U31.1, U32.2; no longer J83.1, U27.2
- net GPIO41: now also J65.1, U31.2; no longer J84.1, U27.3
- net GPIO42: now also J66.1, U31.3; no longer U29.1, U30.2
- net GPIO43: now also U31.5, U33.P8; no longer J89.1, U29.2
- net GPIO44: now also U34.1, U35.2; no longer J90.1, U29.3
- net GPIO45: now also J71.1, U34.2; no longer U31.1, U32.2
- net GPIO46: now also J72.1, U34.3; no longer J95.1, U31.2
- net GPIO47: now also U34.5, U36.P8; no longer J96.1, U31.3
- net GPIO48: now also U37.1, U38.2; no longer U33.1, U34.2
- net GPIO49: now also J77.1, U37.2; no longer J101.1, U33.2
- net GPIO5: now also J11.1, U4.2; no longer J12.1, U3.3
- net GPIO50: now also J78.1, U37.3; no longer J102.1, U33.3
- net GPIO51: now also U37.5, U39.P8; no longer U35.1, U36.2
- net GPIO52: now also U40.1, U41.2; no longer J107.1, U35.2
- net GPIO53: now also J83.1, U40.2; no longer J108.1, U35.3
- net GPIO54: now also J84.1, U40.3; no longer U37.1, U38.2
- net GPIO55: now also U40.5, U42.P8; no longer J113.1, U37.2
- net GPIO56: now also U43.1, U44.2; no longer J114.1, U37.3
- net GPIO57: now also J89.1, U43.2; no longer U39.1, U40.2
- net GPIO58: now also J90.1, U43.3; no longer J119.1, U39.2
- net GPIO59: now also U43.5, U45.P8; no longer J120.1, U39.3
- net GPIO6: now also J12.1, U4.3; no longer U5.1, U6.2
- net GPIO60: now also U46.1, U47.2; no longer U41.1, U42.2
- net GPIO61: now also J95.1, U46.2; no longer J125.1, U41.2
- net GPIO62: now also J96.1, U46.3; no longer J126.1, U41.3
- net GPIO63: now also U46.5, U48.P8; no longer U43.1, U44.2
- net GPIO64: now also U49.1, U50.2; no longer J131.1, U43.2
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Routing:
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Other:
- board text added: "X02"
- board text removed: "X01"

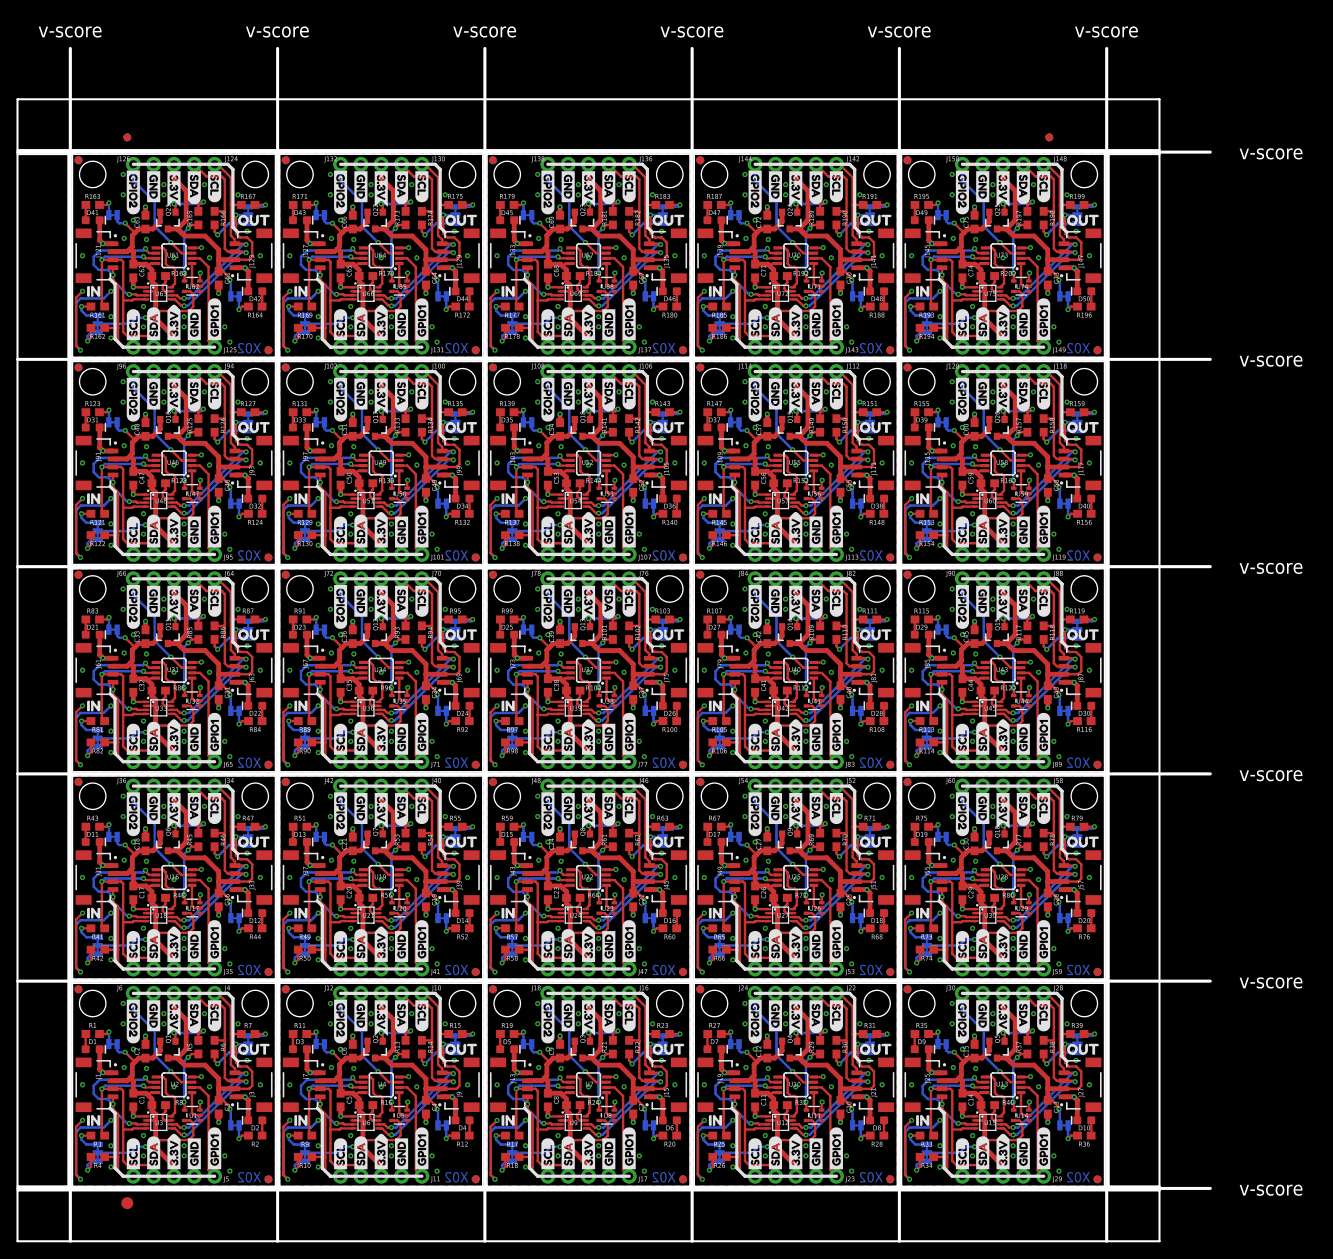
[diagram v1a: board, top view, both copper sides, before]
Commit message: Remove New_Parts.lbr
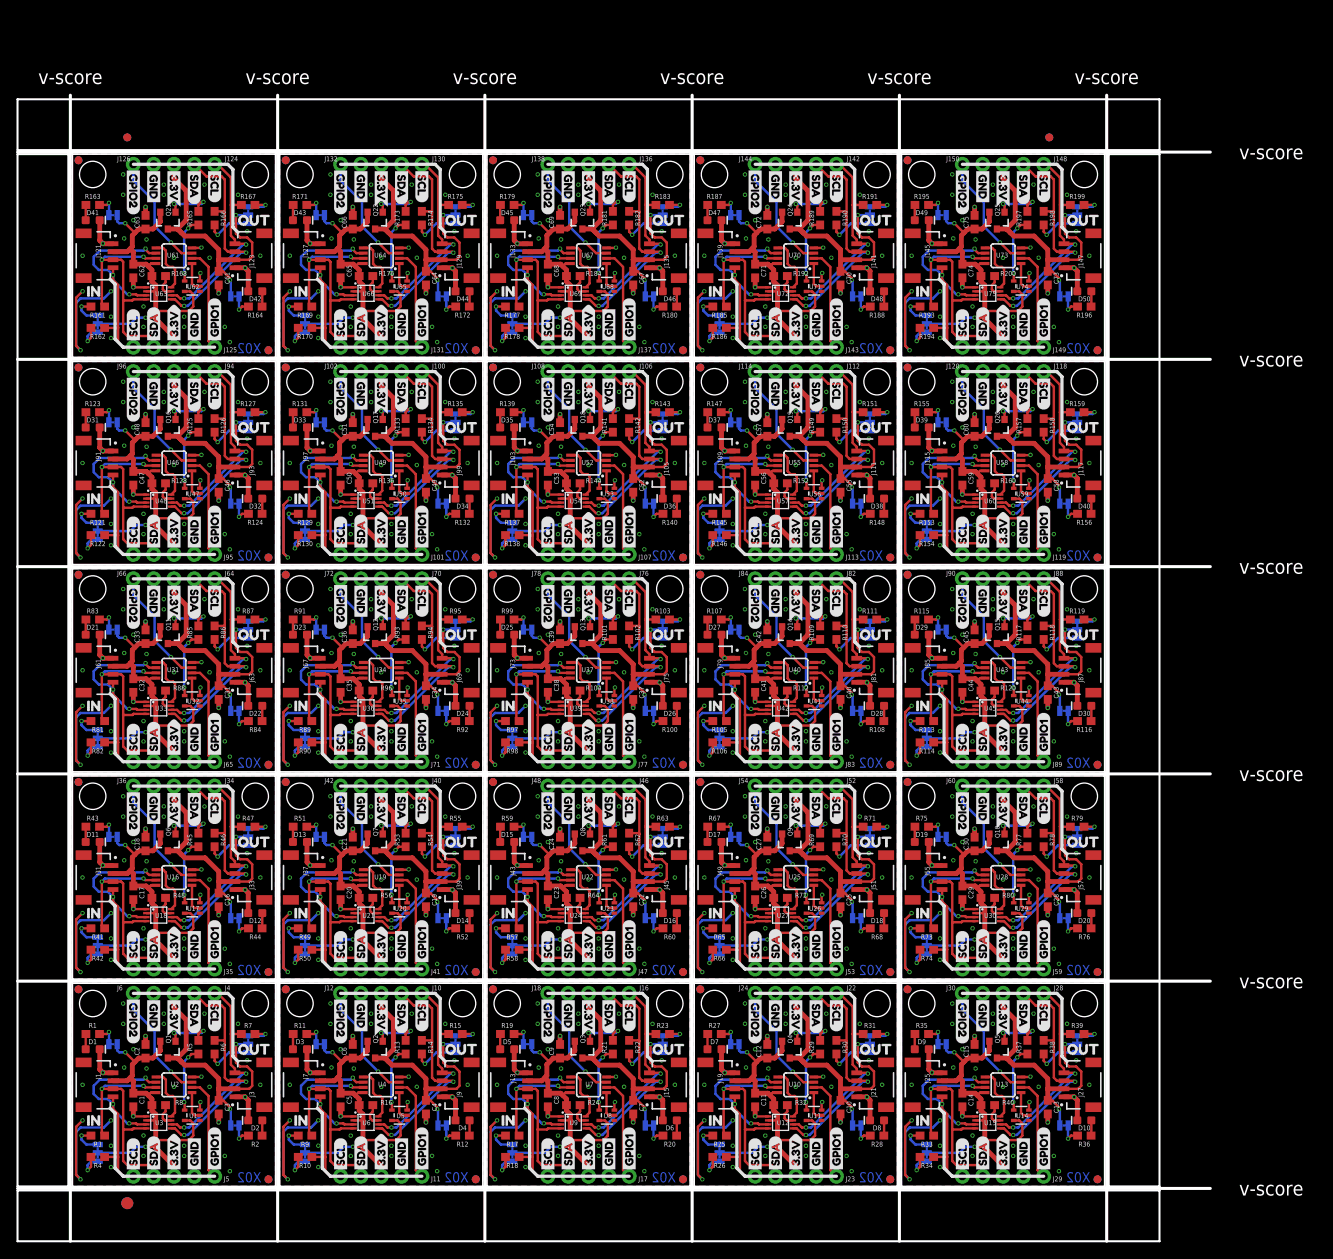
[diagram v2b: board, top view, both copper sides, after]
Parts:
- added E$6: (no value), SparkFun-Retired:FIDUCIAL-1.5X3
- U$121, U$153, U$185, U$217, U$249, U$281, U$313, U$34, U$345, U$377, U$409, U$441, U$473, U$505, U$537, U$569, U$57, U$601, U$633, U$665, U$697, U$729, U$761, U$793, U$89: device Switch:SWITCH0 -> switch:SWITCH0
- U10, U13, U16, U19, U2, U22, U25, U28, U31, U34, U37, U4, U40, U43, U46, U49, U52, U55, U58, U61, U64, U67, U7, U70, U73: device New_Parts:MSOP8 -> SparkFun-IC-Conversion:MSOP8
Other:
- board size 149.1 x 149.1 mm -> 149.1 x 143.3 mm
